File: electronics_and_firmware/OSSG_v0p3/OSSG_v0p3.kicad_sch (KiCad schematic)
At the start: 75 parts, among them IC1 DW01A, J1 USB_B_Micro, J2 External PDM Mic Input, Q1 FS8205A, Q2 Q_NPN_BEC, Q3 Q_NPN_BEC, SW1 SW_SPST, U1 ESP32-PICO-D4, U2 TP4056, U3 XC6222B331MRG, U4 CH9102F, U5 CL7809SS, U6 MP23DB01HPTR

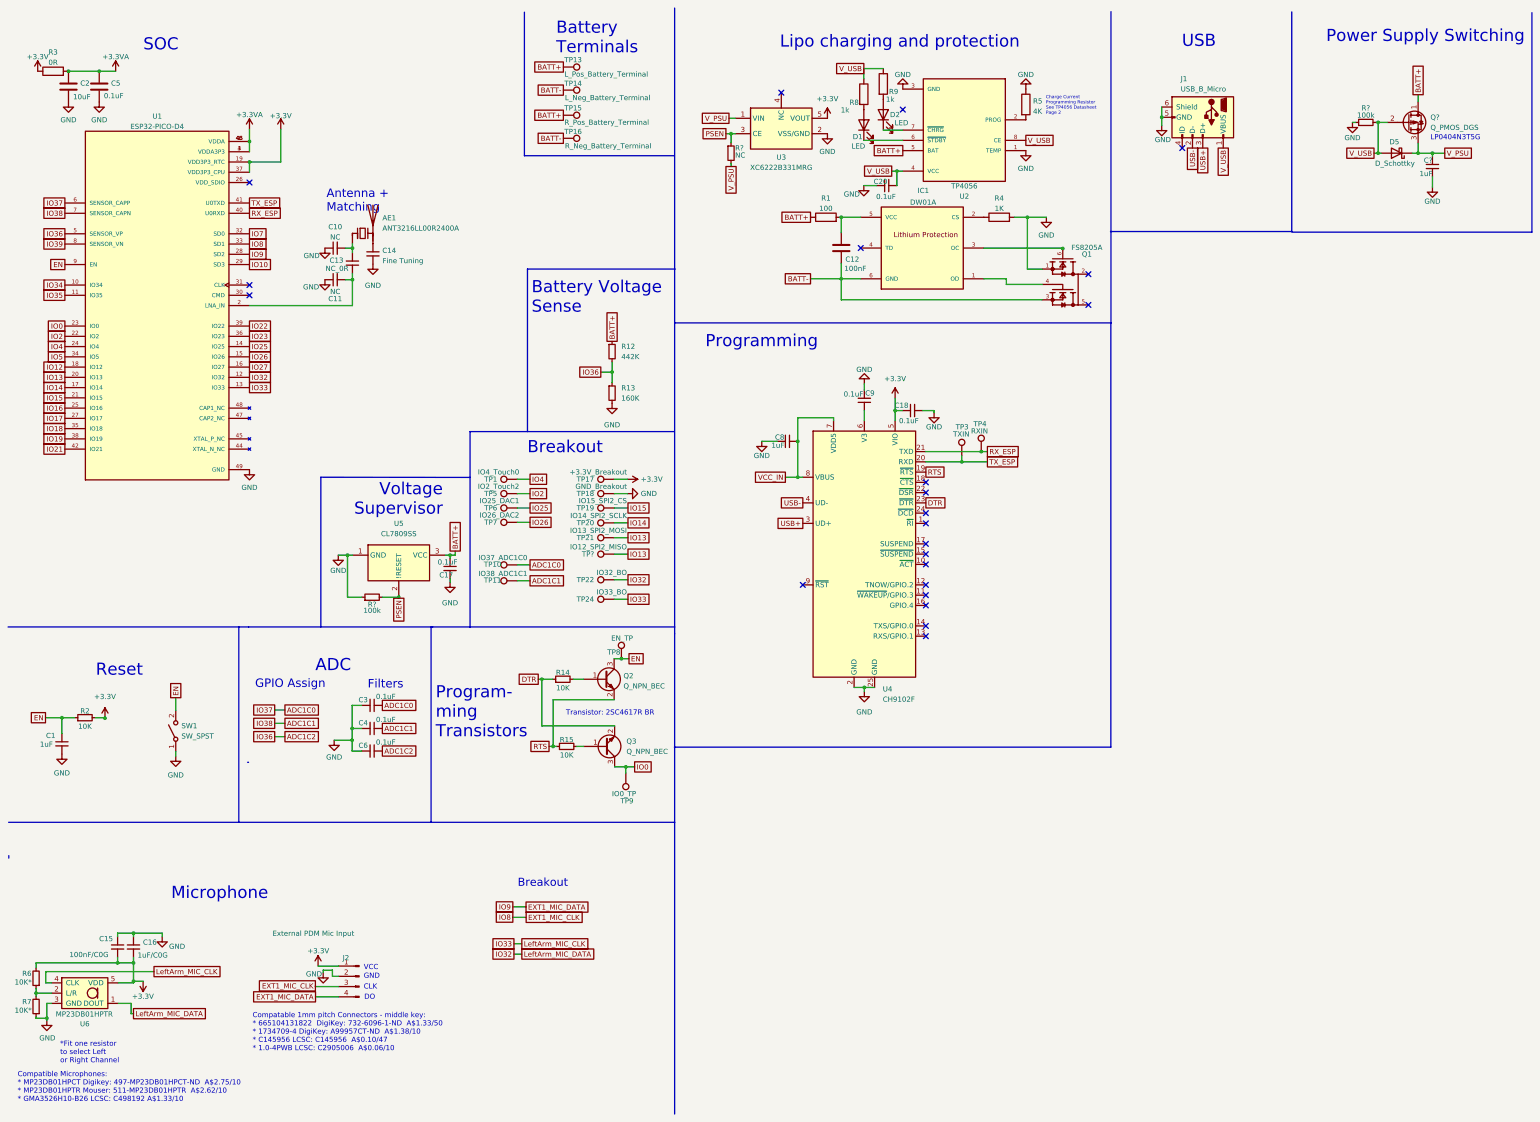
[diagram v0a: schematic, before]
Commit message: layout complete after fixing footprints, adding PSU switching, spreading out breakout points, etc.
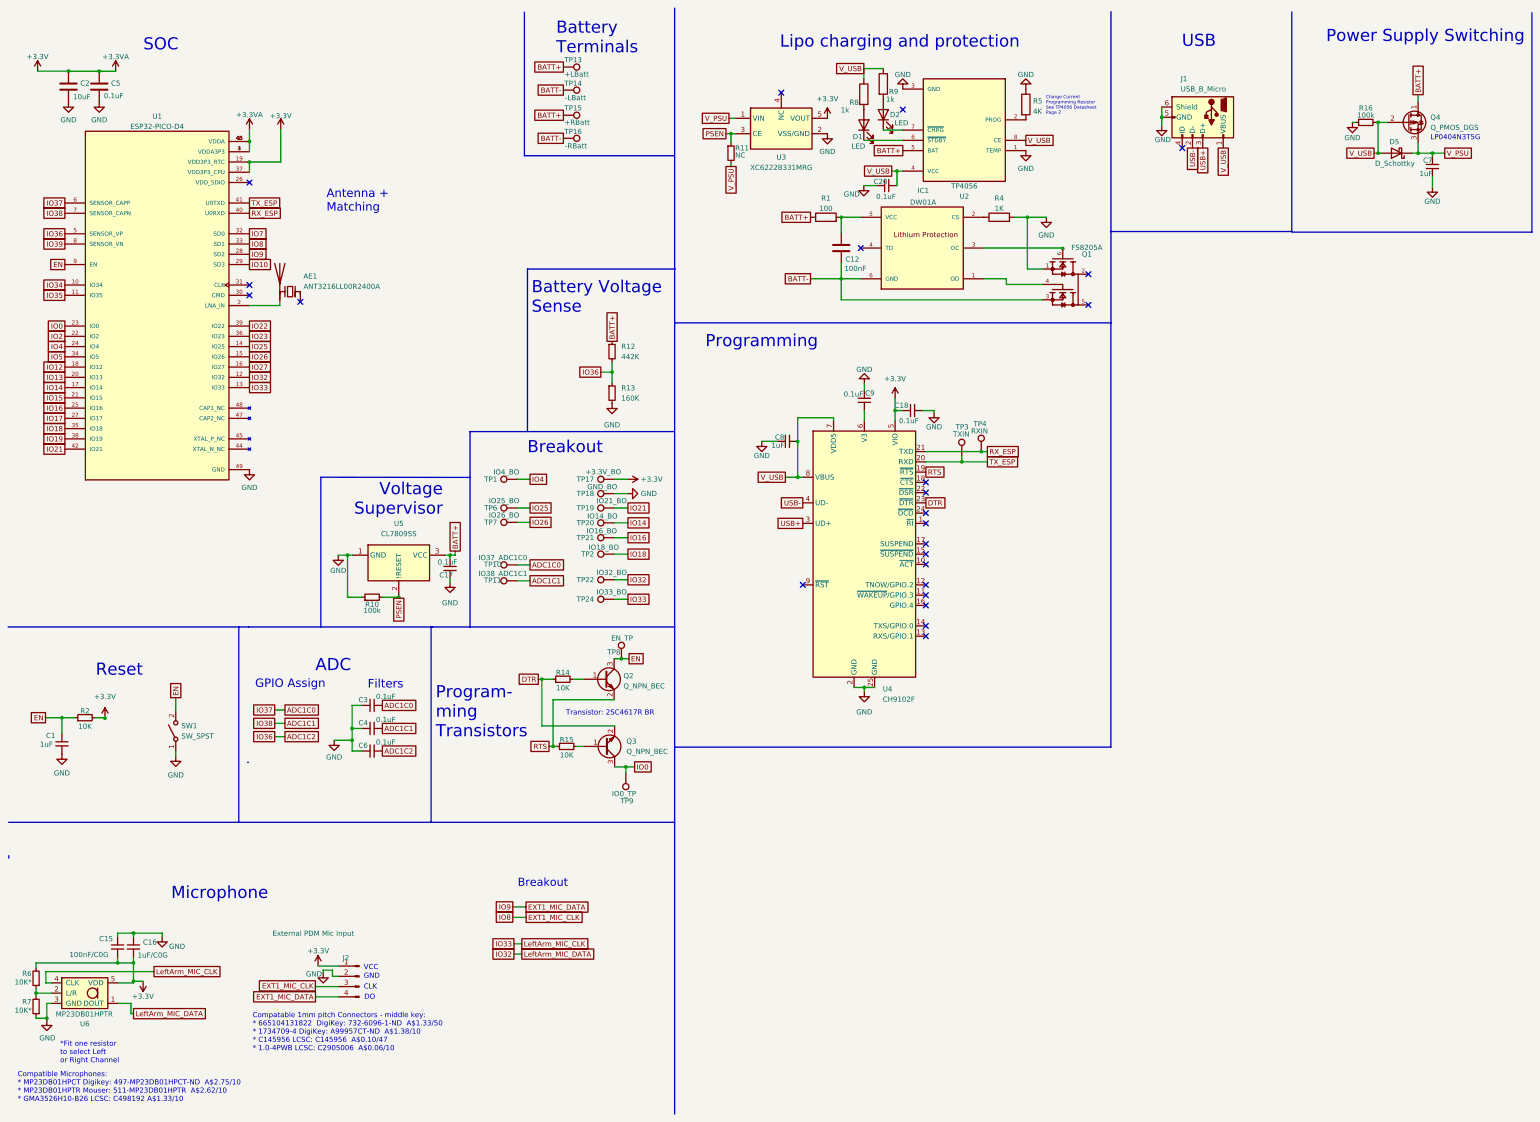
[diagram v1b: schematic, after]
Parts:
- removed C10, C11: NC, Capacitor_SMD:C_0201_0603Metric, symbol Device:C_Small
- removed C13: NC_0R, Capacitor_SMD:C_0201_0603Metric, symbol Device:C_Small
- removed C14: Fine Tuning, Capacitor_SMD:C_0402_1005Metric, symbol Device:C_Small
- removed R3: 0R, Resistor_SMD:R_0402_1005Metric, symbol Device:R
- removed TP5: IO2_Touch2, OSSG_footprints:Breakout_pads, symbol Connector:TestPoint
- AE1: footprint Capacitor_SMD:C_1206_3216Metric -> OSSG_footprints:ANT3216LL00R2400A
- D5: footprint Diode_SMD:D_SOD-123 -> Diode_SMD:D_SOD-323; MPN_LCSC C2937163 -> C109204; Price_LCSC 0.37 -> 0.0163
- TP1: value IO4_Touch0 -> IO4_BO
- TP13: value L_Pos_Battery_Terminal -> +LBatt
- TP14: value L_Neg_Battery_Terminal -> -LBatt
- TP15: value R_Pos_Battery_Terminal -> +RBatt
- TP16: value R_Neg_Battery_Terminal -> -RBatt
- TP17: value +3.3V_Breakout -> +3.3V_BO
- TP18: value GND_Breakout -> GND_BO
- TP19: value IO15_SPI2_CS -> IO21_BO
- TP2: renamed from TP?; value IO12_SPI2_MISO -> IO18_BO
- TP20: value IO14_SPI2_SCLK -> IO14_BO
- TP21: value IO13_SPI2_MOSI -> IO16_BO
- TP6: value IO25_DAC1 -> IO25_BO
- TP7: value IO26_DAC2 -> IO26_BO
- gave numbers to parts that had none: 5
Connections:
- net VCC_IN is gone; now on net V_USB: C8.2, U4.7 (VDD5), U4.8 (VBUS)
- net IO13: no longer TP2.1, TP21.1
- net IO15: no longer TP19.1
- net IO16: now also TP21.1
- net IO18: now also TP2.1
- net IO21: now also TP19.1
- net at U1.2 (LNA_IN): now also AE1.2 (PCB_Trace)
- no-connect marks 22 -> 23
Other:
- moved on the sheet: AE1

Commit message: make breakout smaller, fix issues with breakouts too close to thermal pad, clean up silk screen, generate gerbers
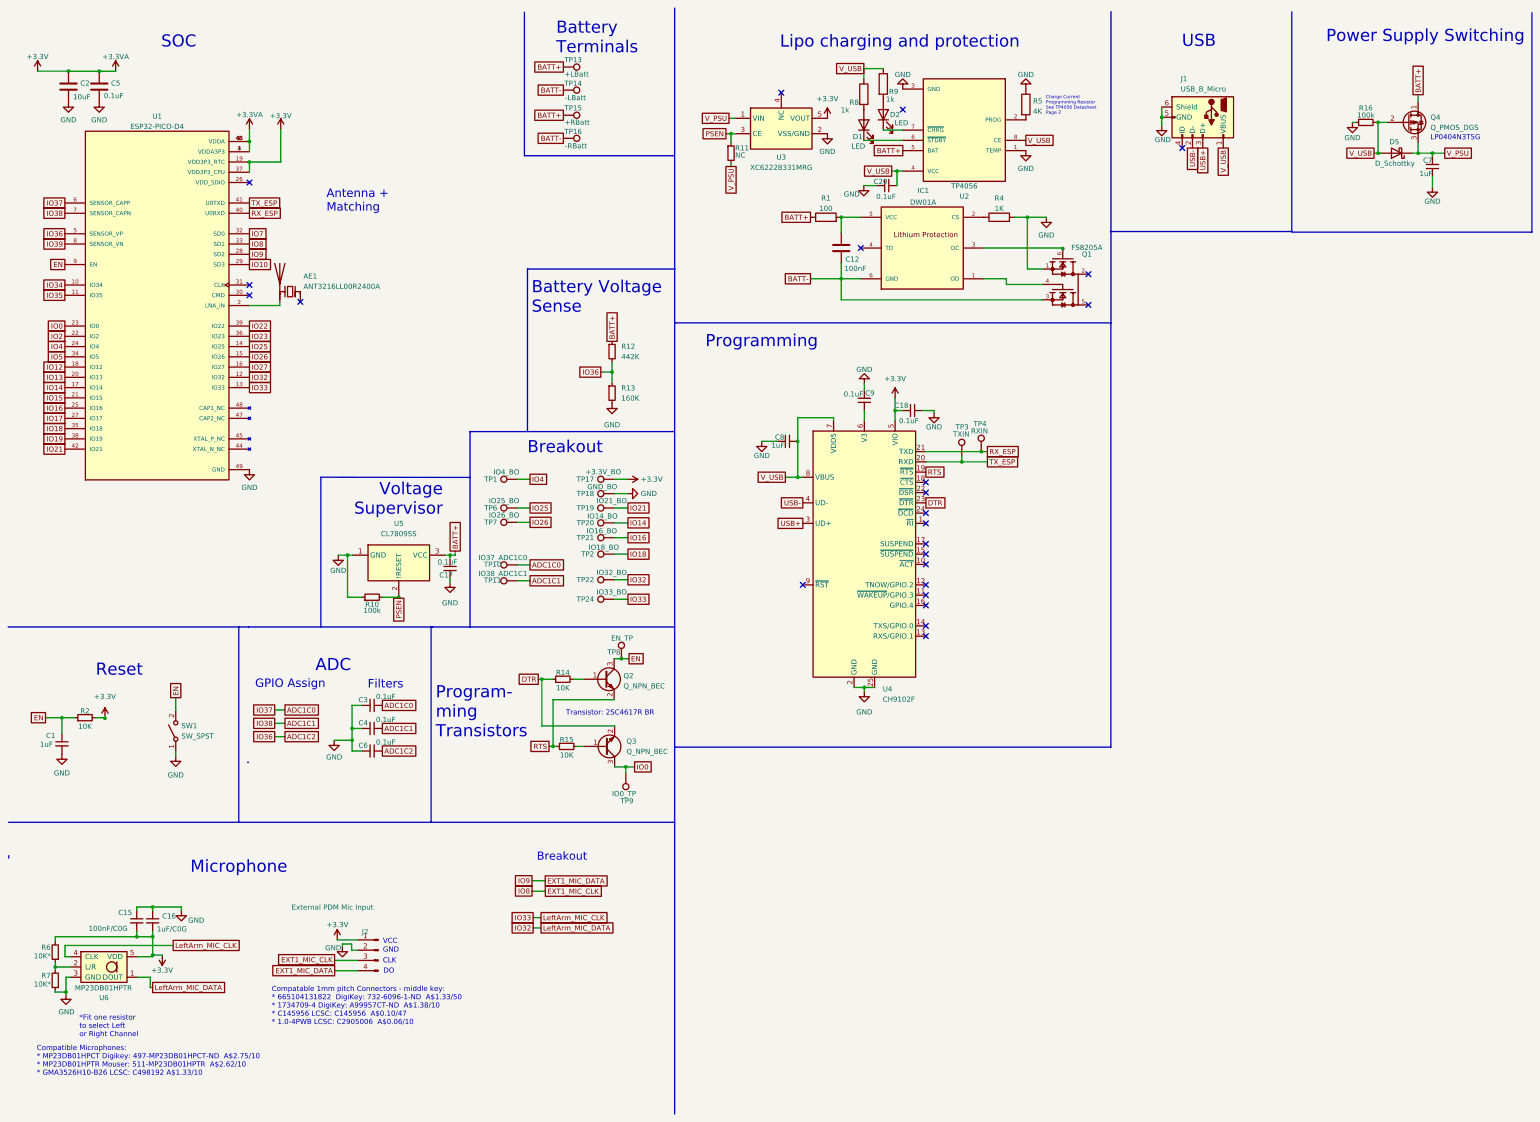
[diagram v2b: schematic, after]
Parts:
- J2: footprint footprints:Solder-4P-Connector -> OSSG_footprints:Solder-4P-Connector
- TP1, TP10, TP11, TP19, TP2, TP20, TP21, TP22, TP24, TP6, TP7: footprint OSSG_footprints:Breakout_pads -> OSSG_footprints:Breakout_pads_small
- U6: footprint footprints:MP23DB01HPTR -> OSSG_footprints:MP23DB01HPTR
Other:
- moved on the sheet: C15, C16, J2, R6, R7, U6

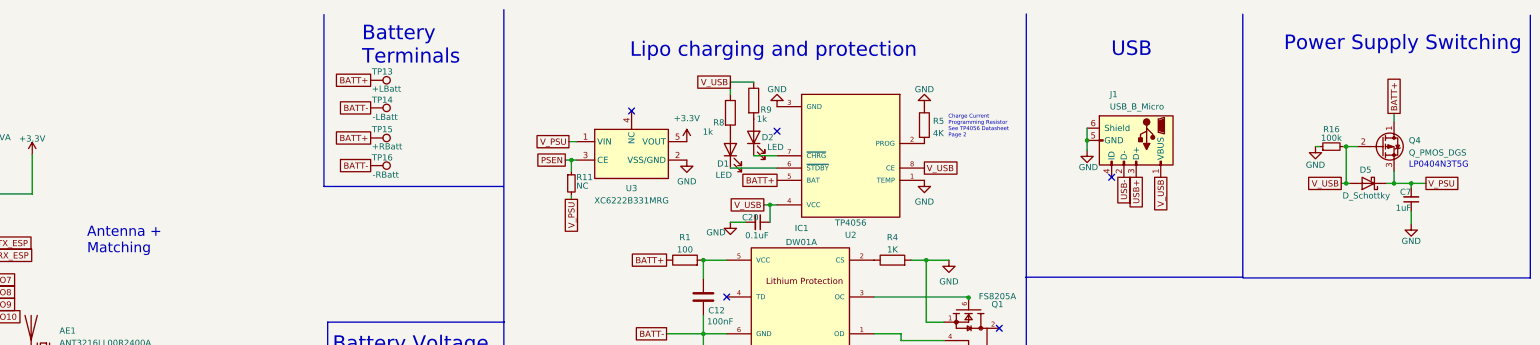
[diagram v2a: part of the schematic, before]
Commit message: change PSU MOSFET symbol from DGS to DSG to match part, cleanup schematic
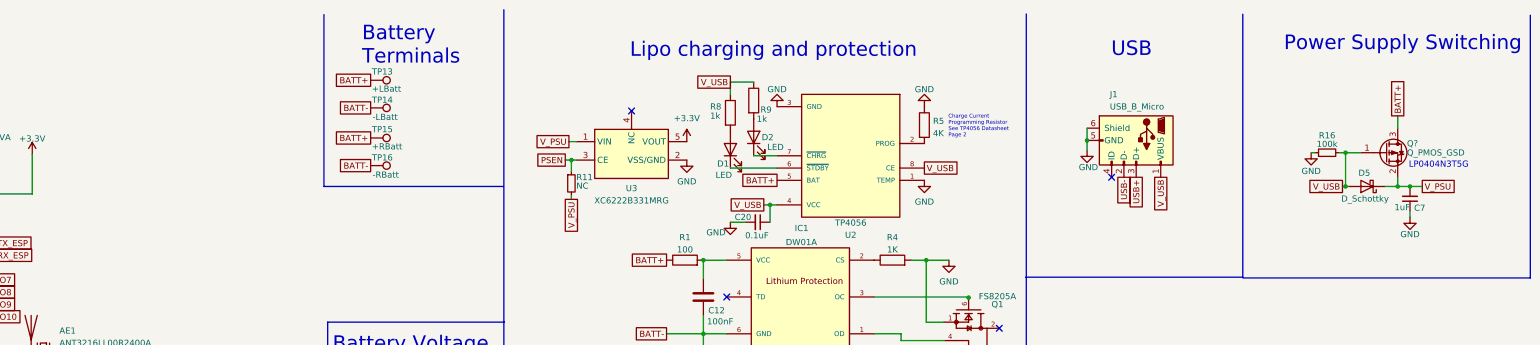
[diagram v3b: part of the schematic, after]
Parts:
- removed Q4: Q_PMOS_DGS, Package_TO_SOT_SMD:SOT-883, symbol Device:Q_PMOS_DGS
- added Q?: Q_PMOS_GSD, symbol Device:Q_PMOS_GSD
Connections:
- net BATT+: now also Q?.3 (D)
- net V_PSU: now also Q?.2 (S)
- net V_USB: now also Q?.1 (G)
- no-connect marks 23 -> 22
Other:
- note removed: "Antenna + Matching"
- moved on the sheet: D5, R16
